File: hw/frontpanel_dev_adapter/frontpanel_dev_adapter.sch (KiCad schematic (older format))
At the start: 1 part

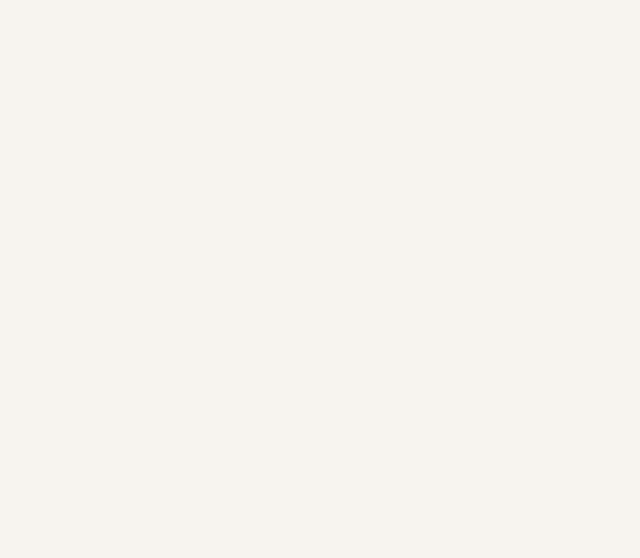
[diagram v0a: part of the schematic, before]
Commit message: "Frontpanel dev-adapter: change some component sizes, add Logo & 4x mounting holes"
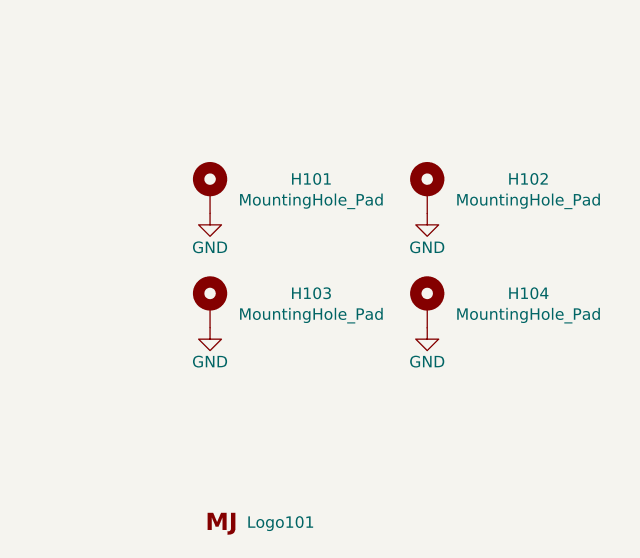
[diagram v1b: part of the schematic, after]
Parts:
- added H101, H102, H103, H104: MountingHole_Pad, MountingHole:MountingHole_3.2mm_M3_ISO7380_Pad, symbol Mechanical:MountingHole_Pad
- added Logo101: Logo_MJ, customlib_mj_fp:MJ_10.3x12.7, symbol customlib_mj:Logo_MJ
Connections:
- new net GND: H101.1, H102.1, H103.1, H104.1
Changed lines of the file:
@@
 	5200 4000 4500 4000
 Connection ~ 4500 4000
+$Comp
+L customlib_mj:Logo_MJ Logo101
+U 1 1 6013DA6B
+P 8700 7050
+F 0 "Logo101" H 8959 7048 50  0000 C CNN
+F 1 "Logo_MJ" H 8700 6950 50  0001 C CNN
+F 2 "customlib_mj_fp:MJ_10.3x12.7" H 8700 7050 50  0001 C CNN
+F 3 "" H 8700 7050 50  0001 C CNN
+	1    8700 7050
+	1    0    0    -1
+$EndComp
+$Comp
+L Mechanical:MountingHole_Pad H101
+U 1 1 6013E8CF
+P 8650 5600
+F 0 "H101" H 9093 5649 50  0000 C CNN
+F 1 "MountingHole_Pad" H 9093 5558 50  0000 C CNN
+F 2 "MountingHole:MountingHole_3.2mm_M3_ISO7380_Pad" H 8650 5600 50  0001 C CNN
+F 3 "~" H 8650 5600 50  0001 C CNN
+	1    8650 5600
+	1    0    0    -1
+$EndComp
+$Comp
+L Mechanical:MountingHole_Pad H102
+U 1 1 6013EAA9
+P 9600 5600
+F 0 "H102" H 10043 5649 50  0000 C CNN
+F 1 "MountingHole_Pad" H 10043 5558 50  0000 C CNN
+F 2 "MountingHole:MountingHole_3.2mm_M3_ISO7380_Pad" H 9600 5600 50  0001 C CNN
+F 3 "~" H 9600 5600 50  0001 C CNN
+	1    9600 5600
+	1    0    0    -1
+$EndComp
+$Comp
+L Mechanical:MountingHole_Pad H103
+U 1 1 6013EFE6
+P 8650 6100
+F 0 "H103" H 9093 6149 50  0000 C CNN
+F 1 "MountingHole_Pad" H 9093 6058 50  0000 C CNN
+F 2 "MountingHole:MountingHole_3.2mm_M3_ISO7380_Pad" H 8650 6100 50  0001 C CNN
+F 3 "~" H 8650 6100 50  0001 C CNN
+	1    8650 6100
+	1    0    0    -1
+$EndComp
+$Comp
+L Mechanical:MountingHole_Pad H104
+U 1 1 6013F3E3
+P 9600 6100
+F 0 "H104" H 10043 6149 50  0000 C CNN
+F 1 "MountingHole_Pad" H 10043 6058 50  0000 C CNN
+F 2 "MountingHole:MountingHole_3.2mm_M3_ISO7380_Pad" H 9600 6100 50  0001 C CNN
+F 3 "~" H 9600 6100 50  0001 C CNN
+	1    9600 6100
+	1    0    0    -1
+$EndComp
+$Comp
+L power:GND #PWR0101
+U 1 1 6013F9C1
+P 8650 5700
+F 0 "#PWR0101" H 8650 5450 50  0001 C CNN
+F 1 "GND" H 8650 5550 50  0000 C CNN
+F 2 "" H 8650 5700 50  0001 C CNN
+F 3 "" H 8650 5700 50  0001 C CNN
+	1    8650 5700
+	1    0    0    -1
+$EndComp
+$Comp
+L power:GND #PWR0102
+U 1 1 6013FECA
+P 9600 5700
+F 0 "#PWR0102" H 9600 5450 50  0001 C CNN
+F 1 "GND" H 9600 5550 50  0000 C CNN
+F 2 "" H 9600 5700 50  0001 C CNN
+F 3 "" H 9600 5700 50  0001 C CNN
+	1    9600 5700
+	1    0    0    -1
+$EndComp
+$Comp
+L power:GND #PWR0104
+U 1 1 60140260
+P 9600 6200
+F 0 "#PWR0104" H 9600 5950 50  0001 C CNN
+F 1 "GND" H 9600 6050 50  0000 C CNN
+F 2 "" H 9600 6200 50  0001 C CNN
+F 3 "" H 9600 6200 50  0001 C CNN
+	1    9600 6200
+	1    0    0    -1
+$EndComp
+$Comp
+L power:GND #PWR0103
+U 1 1 60140486
+P 8650 6200
+F 0 "#PWR0103" H 8650 5950 50  0001 C CNN
+F 1 "GND" H 8650 6050 50  0000 C CNN
+F 2 "" H 8650 6200 50  0001 C CNN
+F 3 "" H 8650 6200 50  0001 C CNN
+	1    8650 6200
+	1    0    0    -1
+$EndComp
 $EndSCHEMATC

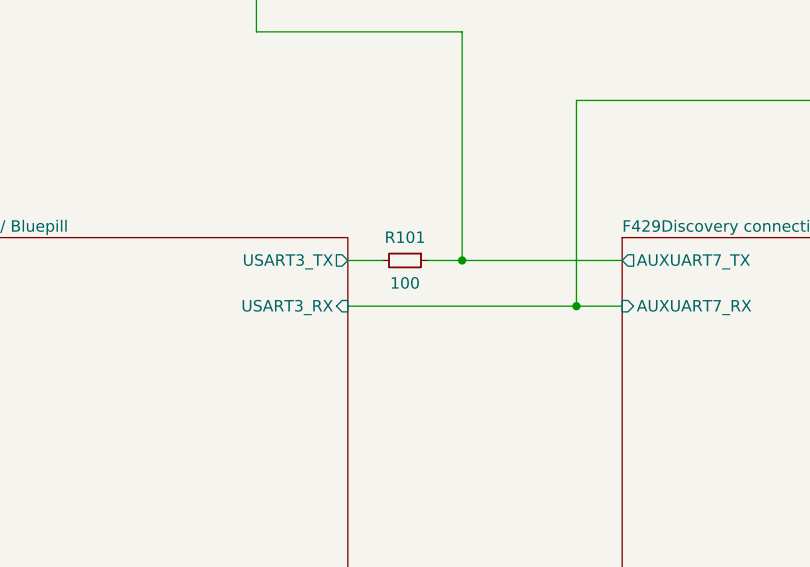
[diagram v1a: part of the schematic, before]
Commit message: Frontpanel dev adapter: Optimize some LCSC components for JLC assembly; add some datasheets. Optimize F103 16MHz xtal routing
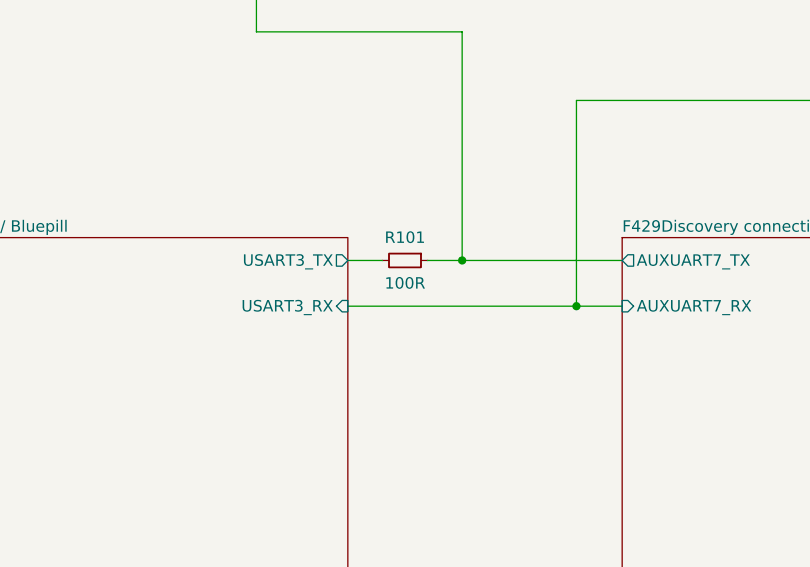
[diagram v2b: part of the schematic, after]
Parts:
- R101: value 100 -> 100R; footprint Resistor_SMD:R_0603_1608Metric -> Resistor_SMD:R_0402_1005Metric
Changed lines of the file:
@@
 P 4250 4000
 F 0 "R101" V 4150 4000 50  0000 C CNN
-F 1 "100" V 4350 4000 50  0000 C CNN
-F 2 "Resistor_SMD:R_0603_1608Metric" H 4250 4000 50  0001 C CNN
+F 1 "100R" V 4350 4000 50  0000 C CNN
+F 2 "Resistor_SMD:R_0402_1005Metric" H 4250 4000 50  0001 C CNN
 F 3 "~" H 4250 4000 50  0001 C CNN
 	1    4250 4000

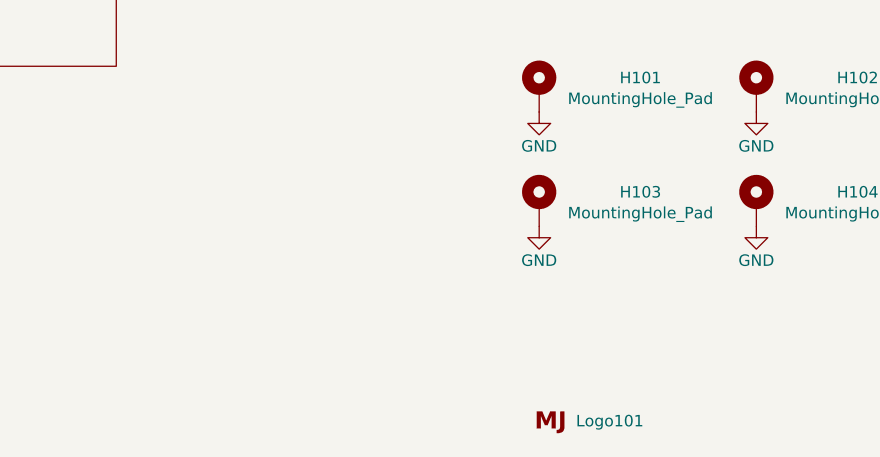
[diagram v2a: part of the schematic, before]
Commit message: FP adapter: Add JLCPCB serial string; tooling holes; route Vin to buck on bottom instead of directly under inductor
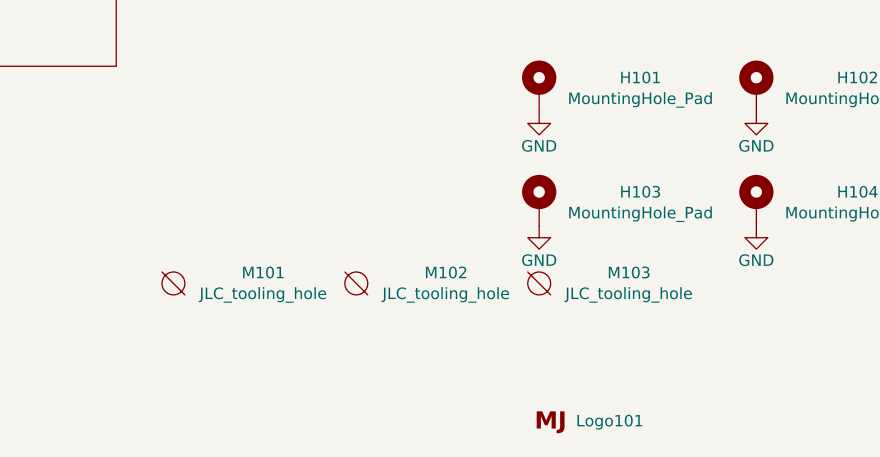
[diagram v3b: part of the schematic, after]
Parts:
- added M101, M102, M103: JLC_tooling_hole, customlib_mj_fp:JLC_tooling-hole, symbol customlib_mj:JLC_tooling_hole
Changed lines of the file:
@@
+	1    0    0    -1
+$EndComp
+$Comp
+L customlib_mj:JLC_tooling_hole M101
+U 1 1 609221CE
+P 7050 6450
+F 0 "M101" H 7443 6496 50  0000 C CNN
+F 1 "JLC_tooling_hole" H 7443 6405 50  0000 C CNN
+F 2 "customlib_mj_fp:JLC_tooling-hole" H 7050 6450 50  0001 C CNN
+F 3 "https://support.jlcpcb.com/article/92-how-to-add-tooling-holes-for-smt-assembly-order" H 7050 6450 50  0001 C CNN
+	1    7050 6450
+	1    0    0    -1
+$EndComp
+$Comp
+L customlib_mj:JLC_tooling_hole M103
+U 1 1 60922604
+P 8650 6450
+F 0 "M103" H 9043 6496 50  0000 C CNN
+F 1 "JLC_tooling_hole" H 9043 6405 50  0000 C CNN
+F 2 "customlib_mj_fp:JLC_tooling-hole" H 8650 6450 50  0001 C CNN
+F 3 "https://support.jlcpcb.com/article/92-how-to-add-tooling-holes-for-smt-assembly-order" H 8650 6450 50  0001 C CNN
+	1    8650 6450
+	1    0    0    -1
+$EndComp
+$Comp
+L customlib_mj:JLC_tooling_hole M102
+U 1 1 609226CE
+P 7850 6450
+F 0 "M102" H 8243 6496 50  0000 C CNN
+F 1 "JLC_tooling_hole" H 8243 6405 50  0000 C CNN
+F 2 "customlib_mj_fp:JLC_tooling-hole" H 7850 6450 50  0001 C CNN
+F 3 "https://support.jlcpcb.com/article/92-how-to-add-tooling-holes-for-smt-assembly-order" H 7850 6450 50  0001 C CNN
+	1    7850 6450
 	1    0    0    -1
 $EndComp

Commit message: FP adapter board: Added LCSC partnumbers to all components to be PnP:ed; Finalized some silk additions; Generated Gerbers, BoM & pnp-files for JCL assembly
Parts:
- R101: LCSC (none) -> C25076
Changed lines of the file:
@@
 F 2 "Resistor_SMD:R_0402_1005Metric" H 4250 4000 50  0001 C CNN
 F 3 "~" H 4250 4000 50  0001 C CNN
+F 4 "C25076" V 4250 4000 50  0001 C CNN "LCSC"
 	1    4250 4000
 	0    1    1    0
